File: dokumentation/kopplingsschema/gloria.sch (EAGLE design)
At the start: 23 parts, among them IC1 74LS125N, U1 SN74AC245DW, U2 SN74AC245DW

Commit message: Updated circuit diagram.
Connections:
- net JTAG_SEN_TCK renamed N$5
- net JTAG_SEN_TDI renamed N$1
- net JTAG_SEN_TDO renamed N$3
- net JTAG_SEN_TMS renamed N$4
- removed net JTAG_STYR_TCK: JTAG_STYR-1.S
- removed net JTAG_STYR_TDI: JTAG_STYR-9.S
- removed net JTAG_STYR_TDO: JTAG_STYR-3.S
- removed net JTAG_STYR_TMS: JTAG_STYR-5.S
- removed net N$11: JTAG_STYR-7.S
- removed net N$12: JTAG_SEN-7.S
- removed net N$13: JTAG_STYR-8.S
- removed net N$14: JTAG_SEN-8.S
- new net N$6: ATMEGA1284P1.TDI/PCINT21, JTAG_STYR-9.S
- new net N$7: ATMEGA1284P1.TDO/PCINT20, JTAG_STYR-3.S
- new net N$8: ATMEGA1284P1.TMS/PCINT19, JTAG_STYR-5.S
- new net N$9: ATMEGA1284P1.TCK/PCINT18, JTAG_STYR-1.S
- net JTAG_STYR_RST: no longer JTAG_STYR-6.S
- net MOTOR_DIR_1: no longer MOTOR-5.S
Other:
- note removed: "JTAG_SEN"
- note removed: "JTAG_STYR"
- moved on the sheet: LINEENABLEMUX1

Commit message: Updated circuit diagrams.
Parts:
- removed BEAGLEBOARD: 057-020-1, con-panduit:057-020-1
- removed LINJESENSOR: 057-026-1, con-panduit:057-026-1
- removed U1, U2: SN74AC245DW, Texas Instruments_By_element14_Batch_1:SN74AC245DW
- added SENSOR_LINE: 057-026-1, con-panduit:057-026-1
- added U$1, U$2: TXB0104SOIC(D), 3DRobotics_Master_Library:TXB0104SOIC(D)
- added X: 057-020-1, con-panduit:057-020-1
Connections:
- net DISTANCERIGHT renamed N$32
- removed net LINE_0_E: LINEENABLEMUX1A.X0, LINJESENSOR-1.S
- removed net LINE_0_OUT: LINEVALUEMUX1A.X0, LINJESENSOR-4.S
- removed net LINE_10_E: LINEENABLEMUX1A.X10, LINJESENSOR-25.S
- removed net LINE_10_OUT: LINEVALUEMUX1A.X10, LINJESENSOR-24.S
- removed net LINE_1_E: LINEENABLEMUX1A.X1, LINJESENSOR-3.S
- removed net LINE_1_OUT: LINEVALUEMUX1A.X1, LINJESENSOR-6.S
- removed net LINE_2_E: LINEENABLEMUX1A.X2, LINJESENSOR-5.S
- removed net LINE_2_OUT: LINEVALUEMUX1A.X2, LINJESENSOR-8.S
- removed net LINE_3_E: LINEENABLEMUX1A.X3, LINJESENSOR-7.S
- removed net LINE_3_OUT: LINEVALUEMUX1A.X3, LINJESENSOR-10.S
- removed net LINE_4_E: LINEENABLEMUX1A.X4, LINJESENSOR-11.S
- removed net LINE_4_OUT: LINEVALUEMUX1A.X4, LINJESENSOR-12.S
- removed net LINE_5_E: LINEENABLEMUX1A.X5, LINJESENSOR-13.S
- removed net LINE_5_OUT: LINEVALUEMUX1A.X5, LINJESENSOR-14.S
- removed net LINE_6_E: LINEENABLEMUX1A.X6, LINJESENSOR-15.S
- removed net LINE_6_OUT: LINEVALUEMUX1A.X6, LINJESENSOR-16.S
- removed net LINE_7_E: LINEENABLEMUX1A.X7, LINJESENSOR-19.S
- removed net LINE_7_OUT: LINEVALUEMUX1A.X7, LINJESENSOR-18.S
- removed net LINE_8_E: LINEENABLEMUX1A.X8, LINJESENSOR-21.S
- removed net LINE_8_OUT: LINEVALUEMUX1A.X8, LINJESENSOR-20.S
- removed net LINE_9_E: LINEENABLEMUX1A.X9, LINJESENSOR-23.S
- removed net LINE_9_OUT: LINEVALUEMUX1A.X9, LINJESENSOR-22.S
- removed net N$2 (its old number): U1.A1
- removed net SEN_CLK: ATMEGA1284P.XTAL2
- removed net SPI_MISO: ATMEGA1284P.MISO/OC3A/PCINT14
- removed net SPI_MOSI: ATMEGA1284P.MOSI/ICP3/PCINT13, U2.B2
- removed net SPI_SCK: ATMEGA1284P.SCK/OC3B/PCINT15, U2.B1
- removed net SPI_SS_SEN: ATMEGA1284P.SS/OC0B/PCINT12, U2.B4
- removed net SPI_SS_STYR: U2.B3
- removed net SS_SEN: BEAGLEBOARD-16.S, U2.A4
- removed net SS_STYR: BEAGLEBOARD-18.S, U2.A3
- removed net STYR_CLK: ATMEGA1284P1.XTAL2
- removed net VCC_BEAGLEBOARD: BEAGLEBOARD-20.S, U1.VCC
- new net N$10: LINEENABLEMUX1A.X0, SENSOR_LINE-1.S
- new net N$11: LINEENABLEMUX1A.X1, SENSOR_LINE-3.S
- new net N$12: LINEENABLEMUX1A.X2, SENSOR_LINE-5.S
- new net N$13: LINEENABLEMUX1A.X3, SENSOR_LINE-7.S
- new net N$14: LINEENABLEMUX1A.X4, SENSOR_LINE-11.S
- new net N$15: LINEENABLEMUX1A.X5, SENSOR_LINE-13.S
- new net N$16: LINEENABLEMUX1A.X6, SENSOR_LINE-15.S
- new net N$17: LINEENABLEMUX1A.X7, SENSOR_LINE-19.S
- new net N$18: LINEENABLEMUX1A.X8, SENSOR_LINE-21.S
- new net N$19: LINEENABLEMUX1A.X9, SENSOR_LINE-23.S
- new net N$20: LINEENABLEMUX1A.X10, SENSOR_LINE-25.S
- new net N$21: LINEVALUEMUX1A.X0, SENSOR_LINE-4.S
- new net N$22: LINEVALUEMUX1A.X1, SENSOR_LINE-6.S
- new net N$23: LINEVALUEMUX1A.X2, SENSOR_LINE-8.S
- new net N$24: LINEVALUEMUX1A.X3, SENSOR_LINE-10.S
- new net N$25: LINEVALUEMUX1A.X4, SENSOR_LINE-12.S
- new net N$26: LINEVALUEMUX1A.X5, SENSOR_LINE-14.S
- new net N$27: LINEVALUEMUX1A.X6, SENSOR_LINE-16.S
- new net N$28: LINEVALUEMUX1A.X7, SENSOR_LINE-18.S
- new net N$29: LINEVALUEMUX1A.X8, SENSOR_LINE-20.S
- new net N$30: LINEVALUEMUX1A.X9, SENSOR_LINE-22.S
- new net N$31: LINEVALUEMUX1A.X10, SENSOR_LINE-24.S
- new net N$33: U$1.OE, U$1.VCCA, U$2.OE, U$2.VCCA, X-20.S
- new net N$35: U$1.A1, X-8.S
- new net N$36: U$1.A2, X-10.S
- new net N$37: U$2.A1, X-12.S
- new net N$38: U$1.A3, X-16.S
- new net N$39: U$1.A4, X-18.S
- new net SS0: ATMEGA1284P1.SS/OC0B/PCINT12, U$1.B4
- new net SS1: ATMEGA1284P.SS/OC0B/PCINT12, U$1.B3
- net GND: now also SENSOR_LINE-17.S, SENSOR_LINE-2.S, SENSOR_LINE-26.S, SENSOR_LINE-9.S, U$1.GND, U$2.GND, X-2.S; no longer LINJESENSOR-17.S, LINJESENSOR-2.S, LINJESENSOR-26.S, LINJESENSOR-9.S, U1.DIR, U1.GND, U1.~OE, U2.GND, U2.~OE
- net JTAG_STYR_RST: now also JTAG_STYR-6.S
- net MISO: now also ATMEGA1284P.MISO/OC3A/PCINT14, ATMEGA1284P1.MISO/OC3A/PCINT14, U$2.B1; no longer BEAGLEBOARD-12.S, U1.B1
- net MOSI: now also ATMEGA1284P.MOSI/ICP3/PCINT13, ATMEGA1284P1.MOSI/ICP3/PCINT13, U$1.B2; no longer BEAGLEBOARD-10.S, U2.A2
- net SCK: now also ATMEGA1284P.SCK/OC3B/PCINT15, ATMEGA1284P1.SCK/OC3B/PCINT15, U$1.B1; no longer BEAGLEBOARD-8.S, U2.A1
- net VCC: now also U$1.VCCB, U$2.VCCB; no longer U2.DIR, U2.VCC
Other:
- note removed: "SENSOR_LINE_ENABLE"
- note removed: "SENSOR_LINE_OUT"
- note removed: "SPI MISO, EJ FÄRDIG"
- note removed: "SPI_SEN"
- note removed: "SPI_STYR"
- note removed: "Saknar EXO 3"

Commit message: Updated circuit diagrams some more.
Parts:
- added C5, C6: 22p, rcl:C-EUC1206
- added C7, C8: 22p, rcl:C-EU025-050X050
- added Q1, Q2: (no value), special:XTAL/S
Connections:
- net MOTOR_DIR_2 renamed N$40
- removed net MOTOR_DIR_1: ATMEGA1284P1.ADC0/PCINT0
- removed net MOTOR_PWM_1: MOTOR-7.S
- removed net MOTOR_PWM_2: MOTOR-8.S
- new net N$34: ATMEGA1284P1.ADC0/PCINT0, MOTOR-5.S
- new net N$41: ATMEGA1284P.XTAL2, C6.1, Q1.2
- new net N$42: ATMEGA1284P1.OC2B/ICP/PCINT30, MOTOR-8.S
- new net N$43: ATMEGA1284P.XTAL1, C5.2, Q1.1
- new net N$44: ATMEGA1284P1.XTAL2, C8.2, Q2.2
- new net N$45: ATMEGA1284P1.XTAL1, C7.2, Q2.1
- new net N$9: ATMEGA1284P1.OC2A/PCINT31, MOTOR-7.S
- net GND: now also C5.1, C6.2, C7.1, C8.1
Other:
- moved on the sheet: C3

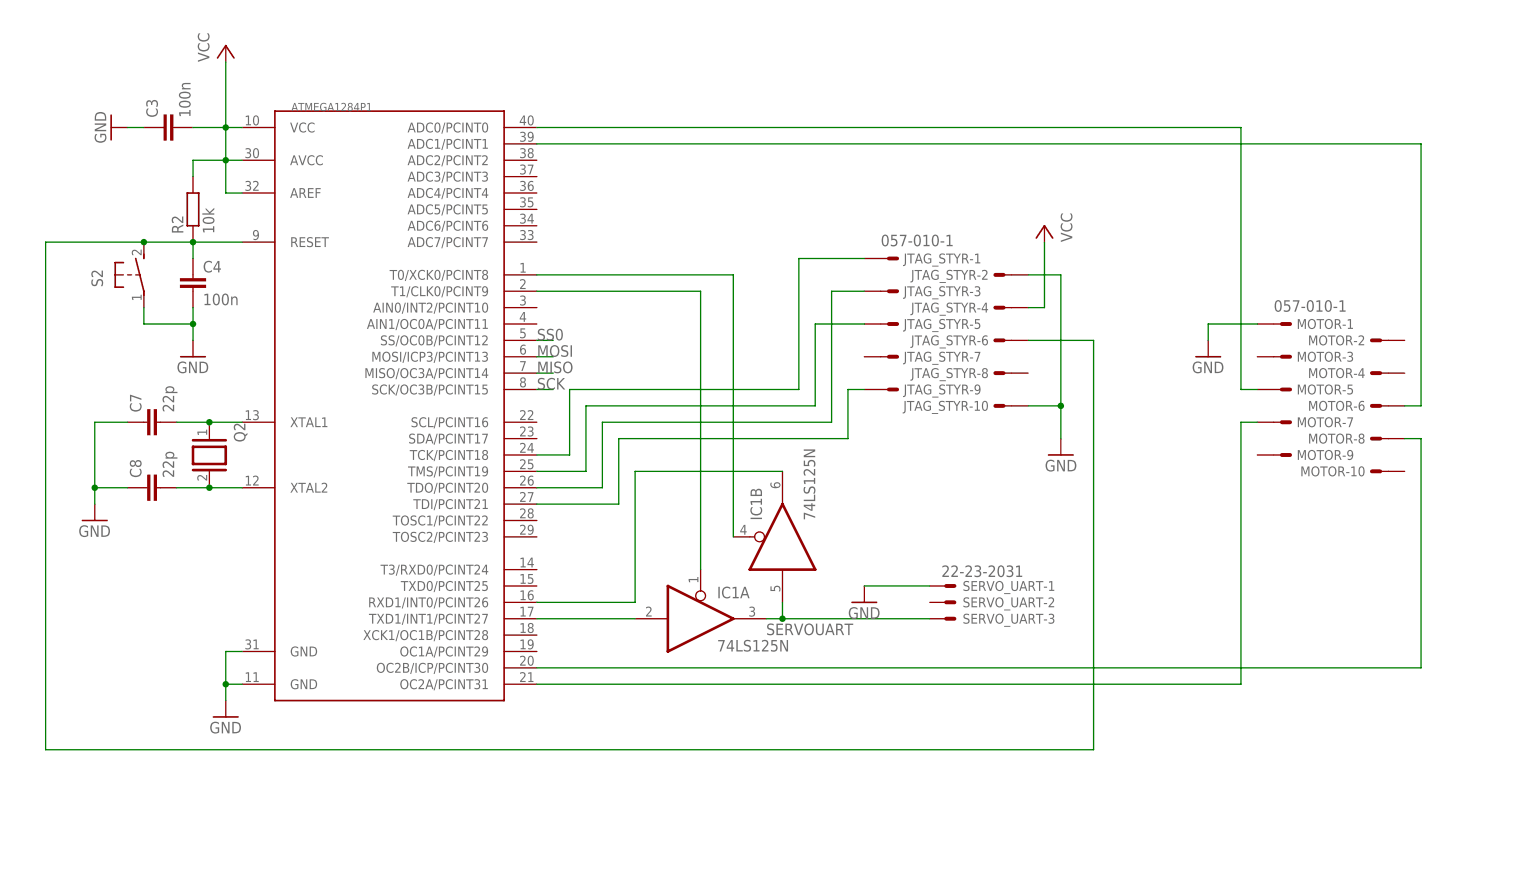
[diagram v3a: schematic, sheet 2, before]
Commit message: Modified motor control.
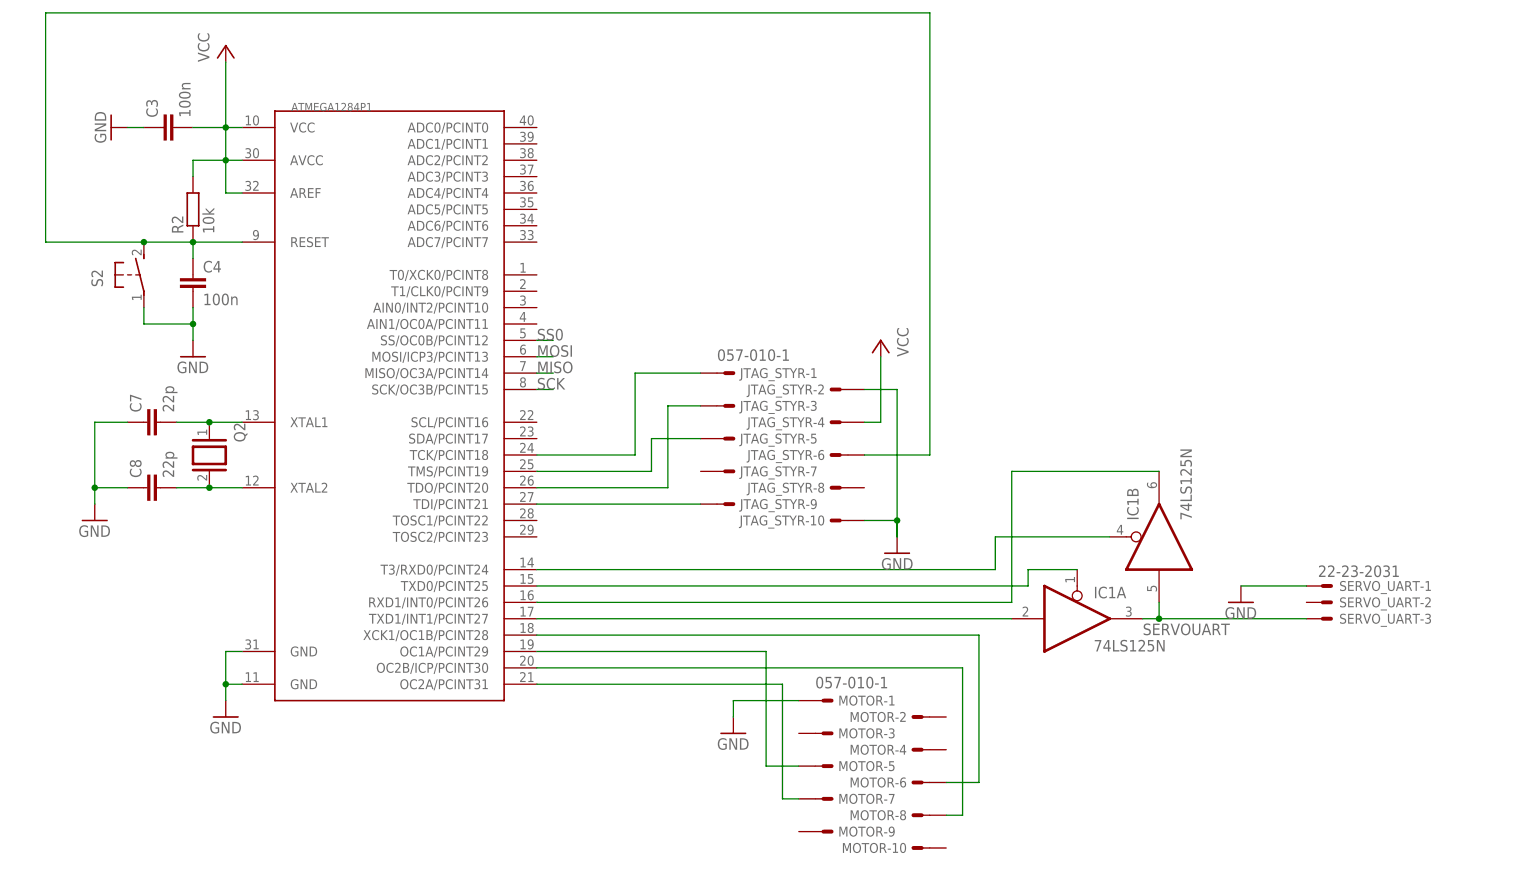
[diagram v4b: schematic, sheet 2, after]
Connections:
- removed net STYR_UART_RX_E: ATMEGA1284P1.T0/XCK0/PCINT8, IC1B.OE
- removed net STYR_UART_TX_E: ATMEGA1284P1.T1/CLK0/PCINT9, IC1A.OE
- new net N$46: ATMEGA1284P1.OC1A/PCINT29, MOTOR-5.S
- new net N$47: ATMEGA1284P1.T3/RXD0/PCINT24, IC1B.OE
- net N$34: now also ATMEGA1284P1.TXD0/PCINT25, IC1A.OE; no longer ATMEGA1284P1.ADC0/PCINT0, MOTOR-5.S
- net N$40: now also ATMEGA1284P1.XCK1/OC1B/PCINT28; no longer ATMEGA1284P1.ADC1/PCINT1
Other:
- moved on the sheet: IC1A, IC1B, JTAG_STYR-1, JTAG_STYR-10, JTAG_STYR-2, JTAG_STYR-3, JTAG_STYR-4, JTAG_STYR-5, JTAG_STYR-6, JTAG_STYR-7, JTAG_STYR-8, JTAG_STYR-9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
